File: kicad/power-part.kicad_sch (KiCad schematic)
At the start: 52 parts, among them Q10 BSS84, Q11 BSS123N, Q12 ZXMP10A17GTA, Q2 IPT015N10N5, Q3 IPT015N10N5, Q4 IPT015N10N5, Q5 IPT015N10N5, Q6 IPT015N10N5, Q7 IPT015N10N5, Q8 IPT015N10N5, Q9 IPT015N10N5

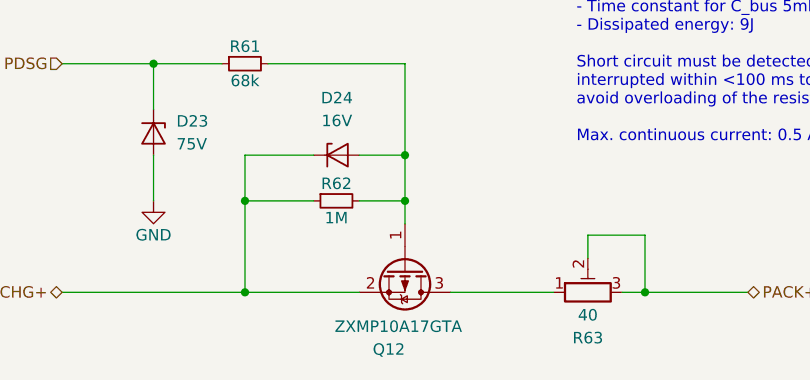
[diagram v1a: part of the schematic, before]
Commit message: Swap D and S of Q12
Fixes #36
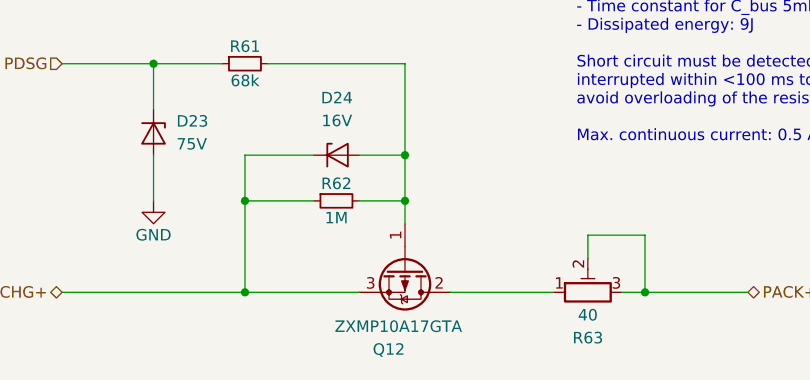
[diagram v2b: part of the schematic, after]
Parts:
- Q12: symbol Device:Q_PMOS_GSD -> Device:Q_PMOS_GDS
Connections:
- net CHG+: now also Q12.3 (S); no longer Q12.2 (S)
- net at R63.1: now also Q12.2 (D); no longer Q12.3 (D)
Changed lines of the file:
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@@
     (pin "2")
   )
-  (symbol (lib_id "Device:Q_PMOS_GSD") (at 220.98 248.92 270) (unit 1)
+  (symbol (lib_id "Device:Q_PMOS_GDS") (at 220.98 248.92 270) (unit 1)
     (in_bom yes) (on_board yes)
     (property "Reference" "Q12" (id 0) (at 220.98 257.81 90)
@@
       (effects (font (size 1.27 1.27)) hide)
     )
-    (property "Datasheet" "" (id 3) (at 220.98 248.92 0))
+    (property "Datasheet" "~" (id 3) (at 220.98 248.92 0)
+      (effects (font (size 1.27 1.27)) hide)
+    )
     (property "Manufacturer" "Diodes Incorporated" (id 4) (at 220.98 248.92 0)
       (effects (font (size 1.524 1.524)) hide)

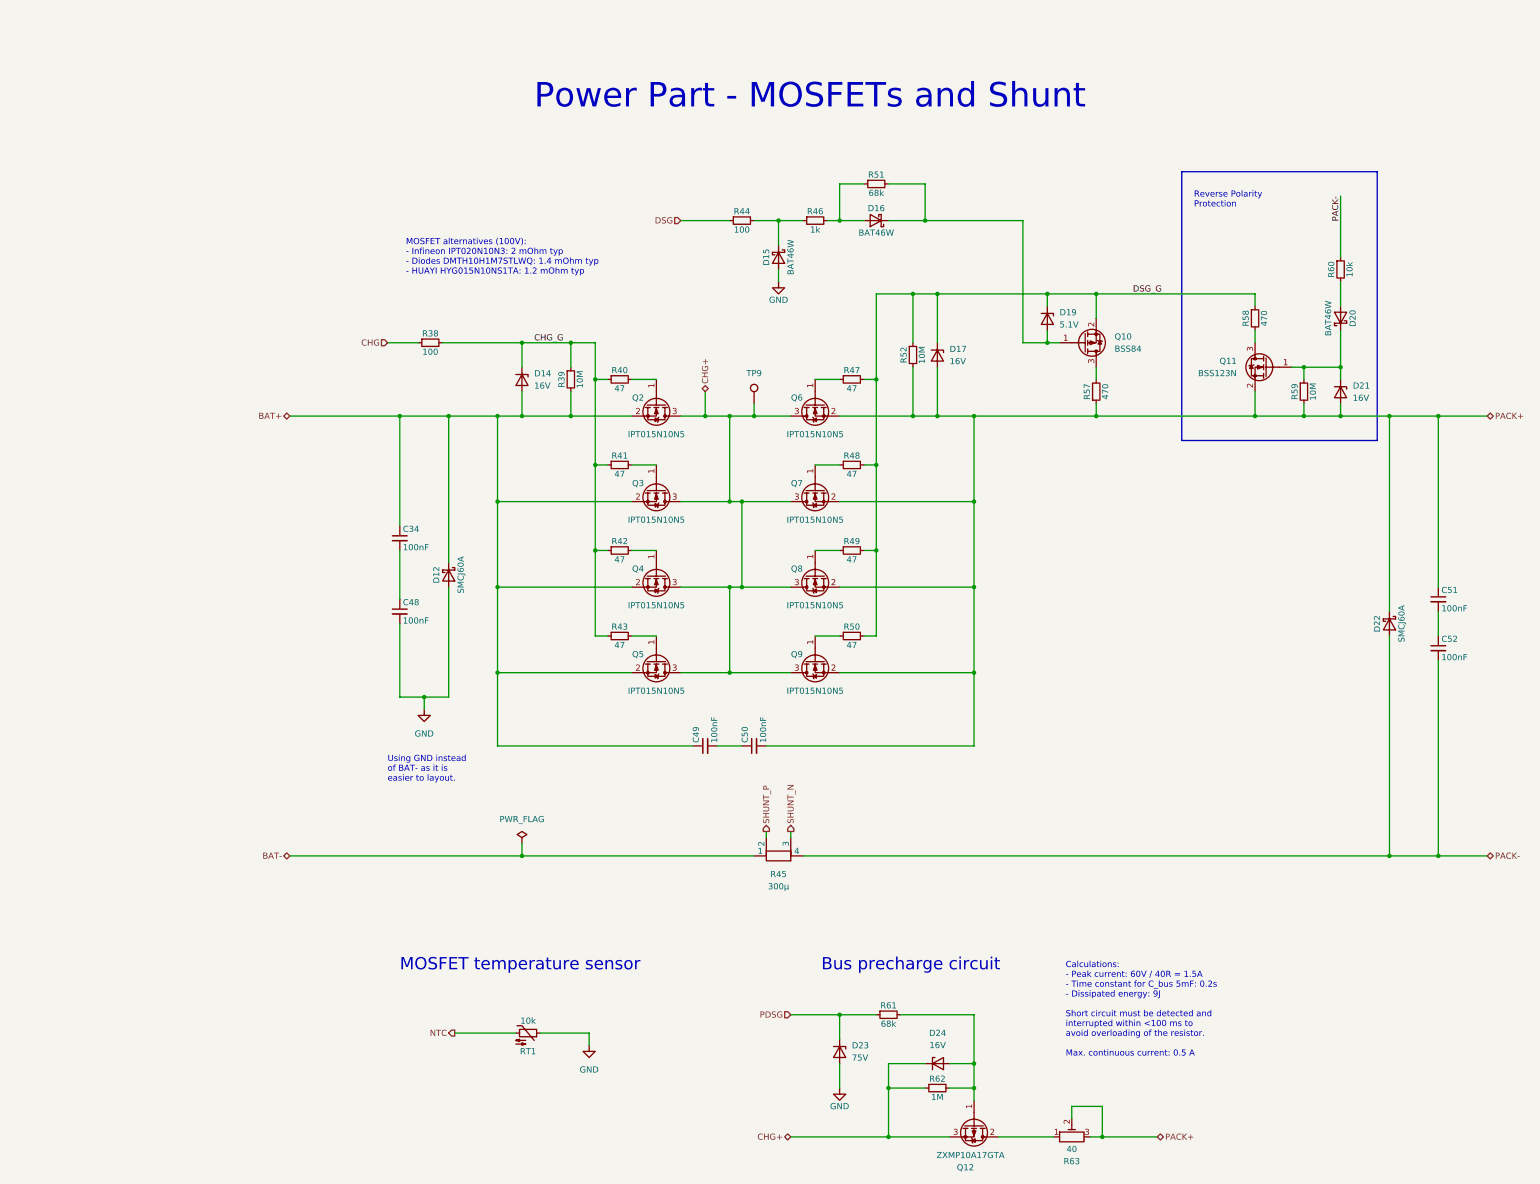
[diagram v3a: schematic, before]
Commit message: All schematics on A4 and small fixes for BOM
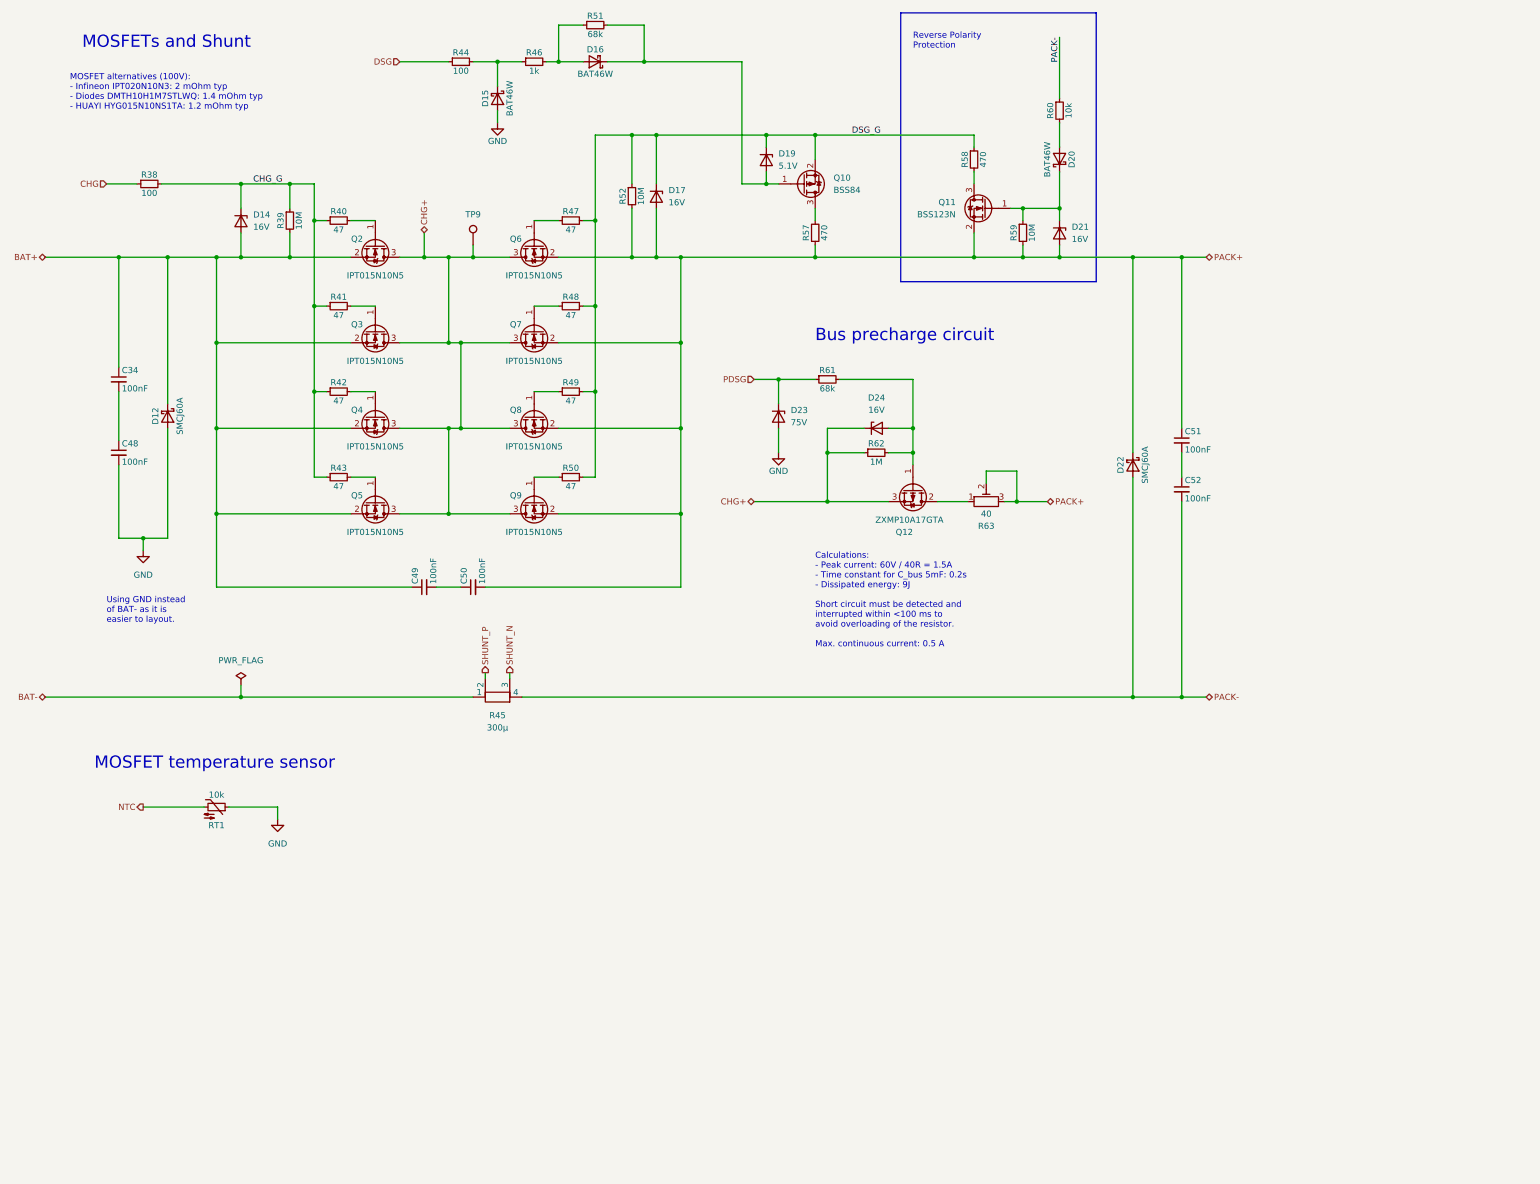
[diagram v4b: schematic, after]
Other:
- note added: "MOSFETs and Shunt"
- note removed: "Power Part - MOSFETs and Shunt"
- moved on the sheet: C34, C48, C49, C50, C51, C52, D12, D14, D15, D16, D17, D19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
